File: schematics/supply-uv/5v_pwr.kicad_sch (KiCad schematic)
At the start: 54 parts, among them Q5 STP13NK60Z, Q6 STP13NK60Z, U10 EL817, U11 UC3525, U12 IRS21867S, U13 TL432DBZ

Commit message: Board#1 schematics rewrited
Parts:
- removed R39, R40: 10K, Resistor_SMD:R_0805_2012Metric, symbol Device:R
- added TP10: +5V_FEEDBACK, Library:TestPoint_Plated_Hole_D1.0mm, symbol Connector:TestPoint
- added TP13: STB_GND, Library:TestPoint_Plated_Hole_D1.0mm, symbol Connector:TestPoint
- added TP14: HV_GND, Library:TestPoint_Plated_Hole_D1.0mm, symbol Connector:TestPoint
- added TP18: +5V_PWR, Library:TestPoint_Plated_Hole_D1.0mm, symbol Connector:TestPoint
- added TP19: +5V_GND, Library:TestPoint_Plated_Hole_D1.0mm, symbol Connector:TestPoint
- renumbered CLR2 to CLR3, D9 to D11, D10 to D12, D11 to D13, D12 to D14, R27 to R29, R28 to R30, R29 to R31, R30 to R32, R31 to R33, R32 to R34, R33 to R35, R34 to R36, R35 to R37, R36 to R38, R37 to R39, R38 to R40, TP4 to TP11, TP5 to TP12, TP6 to TP15, TP7 to TP16, TP8 to TP17
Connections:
- net +5V_PWR: now also TP18.1
- net +5V_PWR_GND: now also TP19.1
- net DCDC_FEEDBACK: now also TP10.1
- net HV_GND: now also U12.4 (COM), TP14.1
- net STB_GND: now also TP13.1; no longer U12.4 (COM)
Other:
- moved on the sheet: D13, D14, NT1, R41, RV2

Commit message: added some protection logic
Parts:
- added C31: 100 nF, Capacitor_SMD:C_0603_1608Metric, symbol Device:C
- added D14: SMBJ3.3A, Diode_SMD:D_SMB, symbol Diode:SMAJ400A
- added F4: 1A, Library:FuseHolder1808, symbol Device:Fuse
- added R31: 220, Resistor_SMD:R_0805_2012Metric, symbol Device:R
- added R39: 0.5R, Resistor_SMD:R_2512_6332Metric, symbol Device:R
- renumbered C28 to C30, C29 to C32, C30 to C33, C31 to C34, C32 to C35, C33 to C36, C34 to C37, C35 to C38, C36 to C39, C37 to C40, C38 to C41, C39 to C42, C40 to C43, C41 to C44, C42 to C45, C43 to C46, C44 to C47, C45 to C48, C46 to C49, D11 to D15, D12 to D16, D13 to D17, D14 to D18, R31 to R32, R32 to R33, R33 to R34, R34 to R35, R35 to R36, R36 to R37, R37 to R38, R38 to R40, R39 to R41, R40 to R42, R41 to R43, U10 to U11, U11 to U12, U12 to U13, U13 to U14
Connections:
- net HV_GND: now also R39.1; no longer Q6.3 (S)
- net HV_VCC: now also F4.1; no longer C40.1, C41.2, C42.2, Q5.2 (D)
- net STB_GND: now also C31.2, D14.2 (A2); no longer U12.10 (SD)
- new net DCDC_CURRENT_SENSE: Q6.3 (S), R31.1, R39.2
- new net DCDC_SHUTDOWN: C31.1, D14.1 (A1), R31.2, U12.10 (SD)
- new net HV_VCC_FUSE: C40.1, C41.2, C42.2, F4.2, Q5.2 (D)

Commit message: start board#1 tracing
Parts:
- TP10, TP18: footprint Library:TestPoint_Plated_Hole_D1.0mm -> TestPoint:TestPoint_Pad_2.0x2.0mm
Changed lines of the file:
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@@
 			)
 		)
-		(property "Footprint" "Library:TestPoint_Plated_Hole_D1.0mm"
+		(property "Footprint" "TestPoint:TestPoint_Pad_2.0x2.0mm"
 			(at 534.67 123.19 0)
 			(effects
@@
 			)
 		)
-		(property "Footprint" "Library:TestPoint_Plated_Hole_D1.0mm"
+		(property "Footprint" "TestPoint:TestPoint_Pad_2.0x2.0mm"
 			(at 111.76 153.67 0)
 			(effects

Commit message: First board routing completed. I will review it few days later and maybe optimize something, but base worki done
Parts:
- removed D14: SMBJ3.3A, Diode_SMD:D_SMB, symbol Diode:SMAJ400A
- removed TP18: +5V_PWR, TestPoint:TestPoint_Pad_2.0x2.0mm, symbol Connector:TestPoint
- removed TP19: +5V_GND, Library:TestPoint_Plated_Hole_D1.0mm, symbol Connector:TestPoint
- added C38: 100 nF, Capacitor_SMD:C_0603_1608Metric, symbol Device:C
- added D14: SM6T30CA, Diode_SMD:D_SMB, symbol Device:D_TVS
- added JP6: Overpower mode, Connector_PinSocket_2.54mm:PinSocket_1x03_P2.54mm_Vertical, symbol Jumper:SolderJumper_3_Open
- NT1: footprint NetTie:NetTie-2_SMD_Pad2.0mm -> NetTie:NetTie-2_SMD_Pad0.5mm
- TP10: footprint TestPoint:TestPoint_Pad_2.0x2.0mm -> TestPoint:TestPoint_Pad_1.0x1.0mm
- renumbered C38 to C39, C39 to C40, C40 to C41, C41 to C42, C42 to C43, C43 to C44, C44 to C45, C45 to C46, C46 to C47, C47 to C48, C48 to C49, C49 to C50, R29 to R31, R31 to R32, R30 to R33, R32 to R34, R33 to R35, R34 to R36, R35 to R37, R36 to R38, R37 to R39, R38 to R40, R39 to R41, R40 to R42, R41 to R43, R42 to R44, R43 to R45
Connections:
- net DCDC_SHUTDOWN: now also JP6.2 (C); no longer C31.1, R32.2
- net HV_GND: now also C31.2, D14.1 (A1)
- net STB_GND: now also C38.2, JP6.1 (A); no longer C31.2
- net STB_VCC: now also C38.1
- new net: C31.1, D14.2 (A2), JP6.3 (B), R32.2
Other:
- moved on the sheet: C31, R32

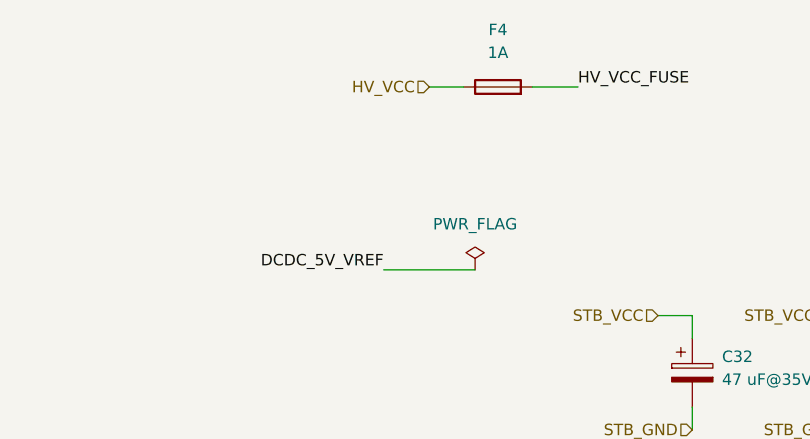
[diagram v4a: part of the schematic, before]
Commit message: first board routed
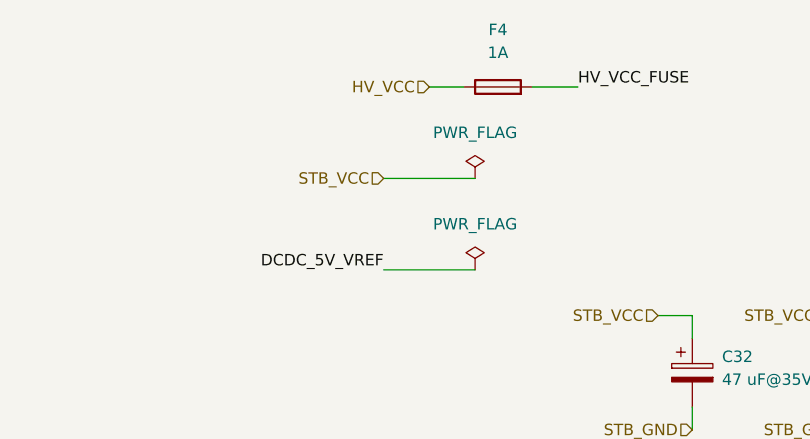
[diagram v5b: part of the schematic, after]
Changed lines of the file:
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@@
 	(wire
 		(pts
+			(xy 62.23 33.02) (xy 72.39 33.02)
+		)
+		(stroke
+			(width 0)
+			(type default)
+		)
+	)
+	(wire
+		(pts
 			(xy 264.16 93.98) (xy 236.22 93.98)
 		)
@@
 		)
 	)
+	(hierarchical_label "STB_VCC"
+		(shape input)
+		(at 62.23 33.02 180)
+		(fields_autoplaced yes)
+		(effects
+			(font
+				(size 1.27 1.27)
+			)
+			(justify right)
+		)
+	)
 	(hierarchical_label "HV_GND"
 		(shape input)
@@
 		(dnp no)
 		(fields_autoplaced yes)
-		(property "Reference" "#FLG012"
+		(property "Reference" "#FLG013"
 			(at 72.39 41.275 0)
 			(effects
@@
 			(project "supply-uv"
 				(path "/ef40850c-d0bf-4cba-961b-9aba418f8e73/c057ed5d-9c60-40b5-98c1-144531018637"
-					(reference "#FLG012")
+					(reference "#FLG013")
 					(unit 1)
 				)
@@
 					(unit 1)
 				)
+			)
+		)
+	)
+	(symbol
+		(lib_id "power:PWR_FLAG")
+		(at 72.39 33.02 0)
+		(unit 1)
+		(exclude_from_sim no)
+		(in_bom yes)
+		(on_board yes)
+		(dnp no)
+		(fields_autoplaced yes)
+		(property "Reference" "#FLG012"
+			(at 72.39 31.115 0)
+			(effects
+				(font
+					(size 1.27 1.27)
+				)
+				(hide yes)
+			)
+		)
+		(property "Value" "PWR_FLAG"
+			(at 72.39 27.94 0)
+			(effects
+				(font
+					(size 1.27 1.27)
+				)
+			)
+		)
+		(property "Footprint" ""
+			(at 72.39 33.02 0)
+			(effects
+				(font
+					(size 1.27 1.27)
+				)
+				(hide yes)
+			)
+		)
+		(property "Datasheet" "~"
+			(at 72.39 33.02 0)
+			(effects
+				(font
+					(size 1.27 1.27)
+				)
+				(hide yes)
+			)
+		)
+		(property "Description" "Special symbol for telling ERC where power comes from"
+			(at 72.39 33.02 0)
+			(effects
+				(font
+					(size 1.27 1.27)
+				)
+				(hide yes)
+			)
+		)
+		(pin "1"
+		)
+		(instances
+			(project "supply-uv"
+				(path "/ef40850c-d0bf-4cba-961b-9aba418f8e73/c057ed5d-9c60-40b5-98c1-144531018637"
+					(reference "#FLG012")
+					(unit 1)
+				)

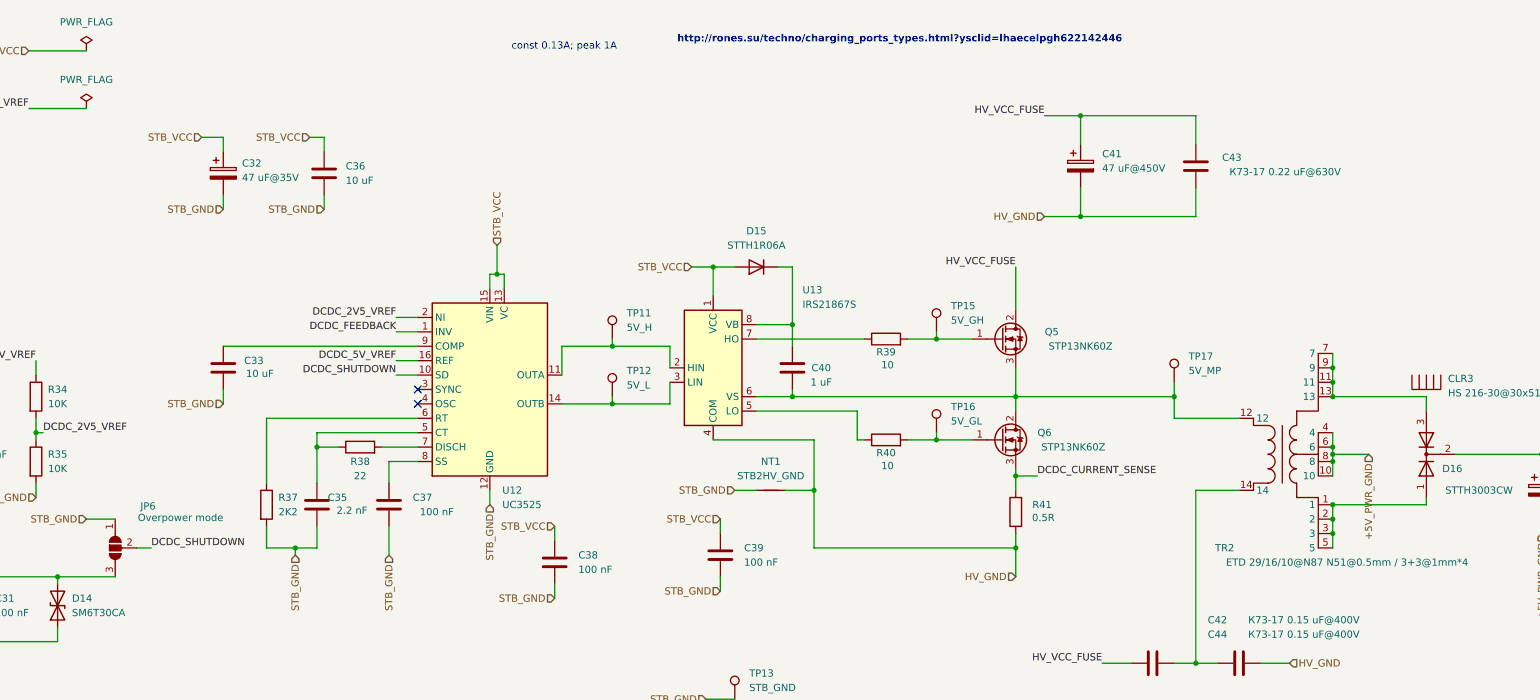
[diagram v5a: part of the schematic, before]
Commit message: some changes in board routing
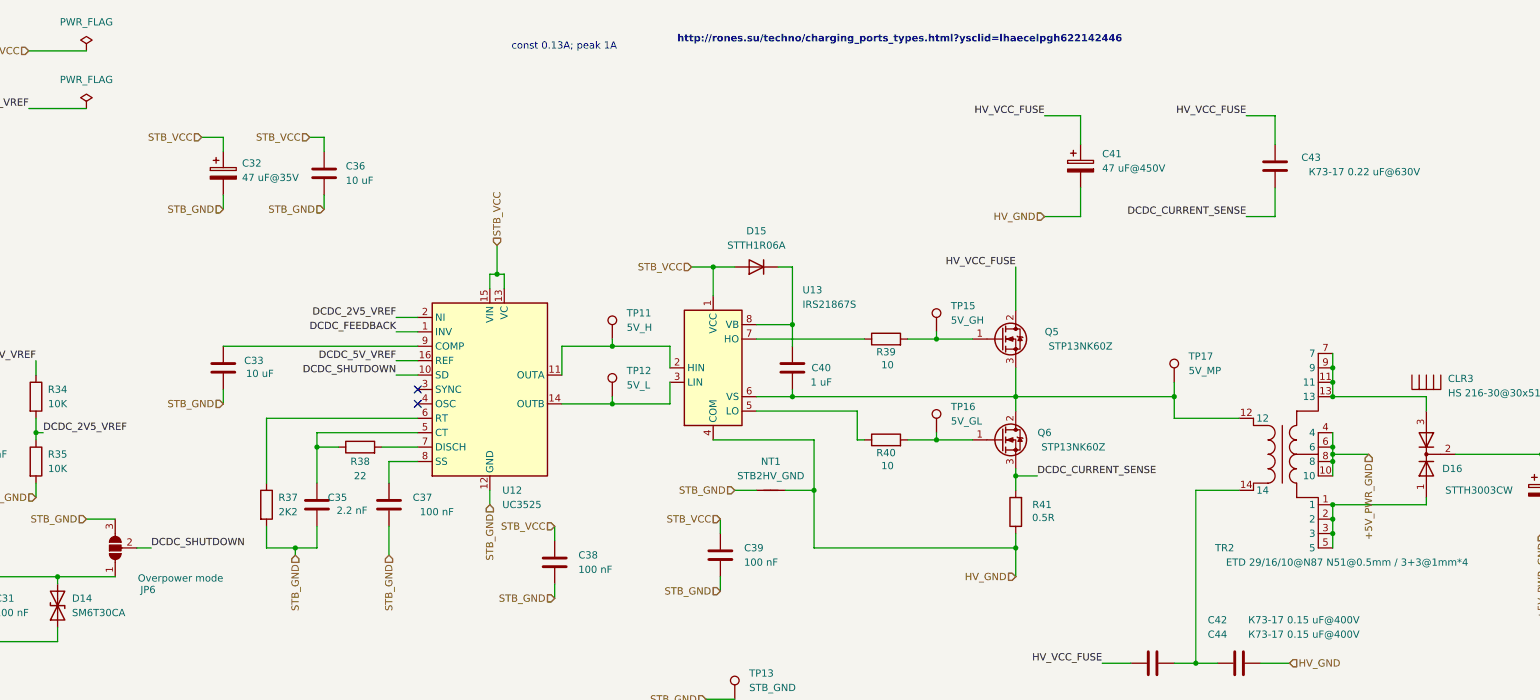
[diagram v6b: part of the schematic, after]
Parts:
- JP6: footprint Connector_PinSocket_2.54mm:PinSocket_1x03_P2.54mm_Vertical -> Jumper:SolderJumper-3_P1.3mm_Bridged2Bar12_RoundedPad1.0x1.5mm_NumberLabels
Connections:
- net DCDC_CURRENT_SENSE: now also C43.1
- net HV_GND: no longer C43.1
- net STB_GND: now also JP6.3 (B); no longer JP6.1 (A)
- net at C31.1, D14.2 (A2), R32.2: now also JP6.1 (A); no longer JP6.3 (B)
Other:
- moved on the sheet: C43
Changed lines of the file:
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@@
 	)
 	(junction
-		(at 247.65 44.45)
+		(at 222.25 101.6)
 		(diameter 0)
 		(color 0 0 0 0)
 	)
 	(junction
-		(at 222.25 101.6)
+		(at 67.31 125.73)
 		(diameter 0)
 		(color 0 0 0 0)
@@
 	)
 	(junction
-		(at 247.65 62.23)
-		(diameter 0)
-		(color 0 0 0 0)
-	)
-	(junction
 		(at 467.36 104.14)
 		(diameter 0)
@@
 	)
 	(junction
-		(at 67.31 125.73)
-		(diameter 0)
-		(color 0 0 0 0)
-	)
-	(junction
 		(at 372.11 104.14)
 		(diameter 0)
@@
 	(wire
 		(pts
-			(xy 247.65 62.23) (xy 267.97 62.23)
+			(xy 127 87.63) (xy 130.81 87.63)
 		)
 		(stroke
@@
 	(wire
 		(pts
-			(xy 127 87.63) (xy 130.81 87.63)
+			(xy 416.56 104.14) (xy 431.8 104.14)
 		)
 		(stroke
@@
 	(wire
 		(pts
-			(xy 416.56 104.14) (xy 431.8 104.14)
+			(xy 78.74 22.86) (xy 83.82 22.86)
 		)
 		(stroke
@@
 	(wire
 		(pts
-			(xy 78.74 22.86) (xy 83.82 22.86)
+			(xy 264.16 97.79) (xy 275.59 97.79)
 		)
 		(stroke
@@
 	(wire
 		(pts
-			(xy 264.16 97.79) (xy 275.59 97.79)
+			(xy 50.8 137.16) (xy 52.07 137.16)
 		)
 		(stroke
@@
 	(wire
 		(pts
-			(xy 50.8 137.16) (xy 52.07 137.16)
+			(xy 308.61 93.98) (xy 308.61 96.52)
 		)
 		(stroke
@@
 	(wire
 		(pts
-			(xy 308.61 93.98) (xy 308.61 96.52)
+			(xy 276.86 44.45) (xy 281.94 44.45)
 		)
 		(stroke
@@
 	(wire
 		(pts
-			(xy 72.39 115.57) (xy 77.47 115.57)
-		)
-		(stroke
-			(width 0)
-			(type default)
-		)
-	)
-	(wire
-		(pts
 			(xy 104.14 156.21) (xy 104.14 157.48)
 		)
@@
 	(wire
 		(pts
+			(xy 276.86 62.23) (xy 281.94 62.23)
+		)
+		(stroke
+			(width 0)
+			(type default)
+		)
+	)
+	(wire
+		(pts
 			(xy 292.1 91.44) (xy 292.1 93.98)
 		)
@@
 	(wire
 		(pts
-			(xy 267.97 49.53) (xy 267.97 44.45)
+			(xy 281.94 49.53) (xy 281.94 44.45)
 		)
 		(stroke
@@
 	(wire
 		(pts
+			(xy 72.39 115.57) (xy 77.47 115.57)
+		)
+		(stroke
+			(width 0)
+			(type default)
+		)
+	)
+	(wire
+		(pts
 			(xy 52.07 151.13) (xy 52.07 154.94)
 		)
@@
 	(wire
 		(pts
-			(xy 267.97 57.15) (xy 267.97 62.23)
+			(xy 281.94 57.15) (xy 281.94 62.23)
 		)
 		(stroke
@@
 	(wire
 		(pts
-			(xy 267.97 44.45) (xy 247.65 44.45)
-		)
-		(stroke
-			(width 0)
-			(type default)
-		)
-	)
-	(wire
-		(pts
 			(xy 236.22 107.95) (xy 240.03 107.95)
 		)
@@
 	(wire
 		(pts
-			(xy 67.31 125.73) (xy 77.47 125.73)
+			(xy 154.94 127) (xy 154.94 129.54)
 		)
 		(stroke
@@
 	(wire
 		(pts
-			(xy 154.94 127) (xy 154.94 129.54)
+			(xy 146.05 74.93) (xy 146.05 72.39)
 		)
 		(stroke
@@
 	(wire
 		(pts
-			(xy 146.05 74.93) (xy 146.05 72.39)
+			(xy 347.98 114.3) (xy 347.98 118.11)
 		)
 		(stroke
@@
 	(wire
 		(pts
-			(xy 347.98 114.3) (xy 347.98 118.11)
+			(xy 67.31 125.73) (xy 77.47 125.73)
 		)
 		(stroke
@@
 		)
 	)
+	(label "HV_VCC_FUSE"
+		(at 276.86 44.45 180)
+		(fields_autoplaced yes)
+		(effects
+			(font
+				(size 1.27 1.27)
+			)
+			(justify right bottom)
+		)
+	)
 	(label "FEEDBACK"
 		(at 372.11 132.08 180)
@@
 		)
 	)
+	(label "DCDC_CURRENT_SENSE"
+		(at 276.86 62.23 180)
+		(fields_autoplaced yes)
+		(effects
+			(font
+				(size 1.27 1.27)
+			)
+			(justify right bottom)
+		)
+	)
 	(label "DCDC_5V_VREF"
 		(at 63.5 87.63 180)
@@
 	(symbol
 		(lib_id "Device:C")
-		(at 267.97 53.34 180)
+		(at 281.94 53.34 180)
 		(unit 1)
 		(exclude_from_sim no)
@@
 		(dnp no)
 		(property "Reference" "C43"
-			(at 274.32 51.816 0)
+			(at 288.29 51.816 0)
 			(effects
 				(font
@@
 		)
 		(property "Value" "К73-17 0.22 uF@630V"
-			(at 283.718 54.356 0)
+			(at 297.688 54.356 0)
 			(effects
 				(font
@@
 		)
 		(property "Footprint" "Capacitor_THT:C_Axial_L12.0mm_D6.5mm_P20.00mm_Horizontal"
-			(at 267.0048 49.53 0)
+			(at 280.9748 49.53 0)
 			(effects
 				(font
@@
 		)
 		(property "Datasheet" "~"
-			(at 267.97 53.34 0)
+			(at 281.94 53.34 0)
 			(effects
 				(font
@@
 		)
 		(property "Description" "Unpolarized capacitor"
-			(at 267.97 53.34 0)
+			(at 281.94 53.34 0)
 			(effects
 				(font
@@
 		(lib_id "Jumper:SolderJumper_3_Open")
 		(at 77.47 120.65 90)
-		(mirror x)
 		(unit 1)
 		(exclude_from_sim yes)
@@
 		(dnp no)
 		(property "Reference" "JP6"
-			(at 84.582 113.284 90)
+			(at 84.582 128.016 90)
 			(effects
 				(font
@@
 		)
 		(property "Value" "Overpower mode"
-			(at 96.52 115.316 90)
+			(at 96.52 125.984 90)
 			(effects
 				(font
@@
 			)
 		)
-		(property "Footprint" "Connector_PinSocket_2.54mm:PinSocket_1x03_P2.54mm_Vertical"
+		(property "Footprint" "Jumper:SolderJumper-3_P1.3mm_Bridged2Bar12_RoundedPad1.0x1.5mm_NumberLabels"
 			(at 77.47 120.65 0)
 			(effects
